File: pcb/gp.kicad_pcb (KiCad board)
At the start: 2 copper layers, 52.1 x 20.3 mm, 33 parts, among them J1 USB_C_Receptacle_USB2.0, U1 XC6206P332MR, U2 STM32F103CBT6, Y1 8M, Y2 NM (32.768k)

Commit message: Hmmmm
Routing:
- net RST: track 46.5 -> 47.6 mm
- net C14: track 34.1 -> 34.7 mm

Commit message: Hmmmm
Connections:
- J4 pad 1: GND -> +3V3
- J4 pad 2: RST -> GND
- J4 pad 3: BO0 -> +5V
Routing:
- net BO0: track 27.0 -> 24.4 mm
- net RST: track 47.6 -> 45.2 mm
- net +3V3: track 141.7 -> 142.5 mm
- net GND: track 0.79 -> 0.00 mm
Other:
- board text removed: "BO0"

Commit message: Hmmm
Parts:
- moved J1 1.27 mm to (200.0, 101.6)
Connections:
- J3 pad 1: GND -> +3V3
- J3 pad 10: A5 -> A4
- J3 pad 11: A6 -> A5
- J3 pad 12: A7 -> A6
- J3 pad 13: B0 -> A7
- J3 pad 14: B1 -> B0
- J3 pad 15: B2 -> B1
- J3 pad 16: B10 -> B2
- J3 pad 17: B11 -> B10
- J3 pad 19: +5V -> GND
- J3 pad 20: GND -> +5V
- J3 pad 5: A0 -> RST
- J3 pad 6: A1 -> A0
- J3 pad 7: A2 -> A1
- J3 pad 8: A3 -> A2
- J3 pad 9: A4 -> A3
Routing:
- net +5V: track 15.0 -> 80.0 mm
- net RST: track 45.2 -> 32.3 mm, vias 4 -> 3
- net B11: track 12.3 -> 0.00 mm
- net +3V3: track 142.5 -> 148.1 mm
- net B2: track 7.57 -> 10.9 mm
- net A4: track 11.0 -> 7.69 mm, vias 1 -> 0
- net VBUS: track 13.7 -> 10.5 mm
- net A5: track 9.07 -> 5.99 mm, vias 1 -> 0
- net A3: track 11.5 -> 8.66 mm
- net A2: track 11.6 -> 9.02 mm
- net Net-(J1-PadA7): track 5.22 -> 7.76 mm
- net A1: track 13.9 -> 11.4 mm
- net A0: track 16.2 -> 13.7 mm
- net B10: track 10.4 -> 12.5 mm
- net B1: track 6.19 -> 7.99 mm
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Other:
- board text removed: "B11"

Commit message: Updated pcb
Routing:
- net A11: track 26.0 -> 27.7 mm
- net A12: track 30.1 -> 31.6 mm

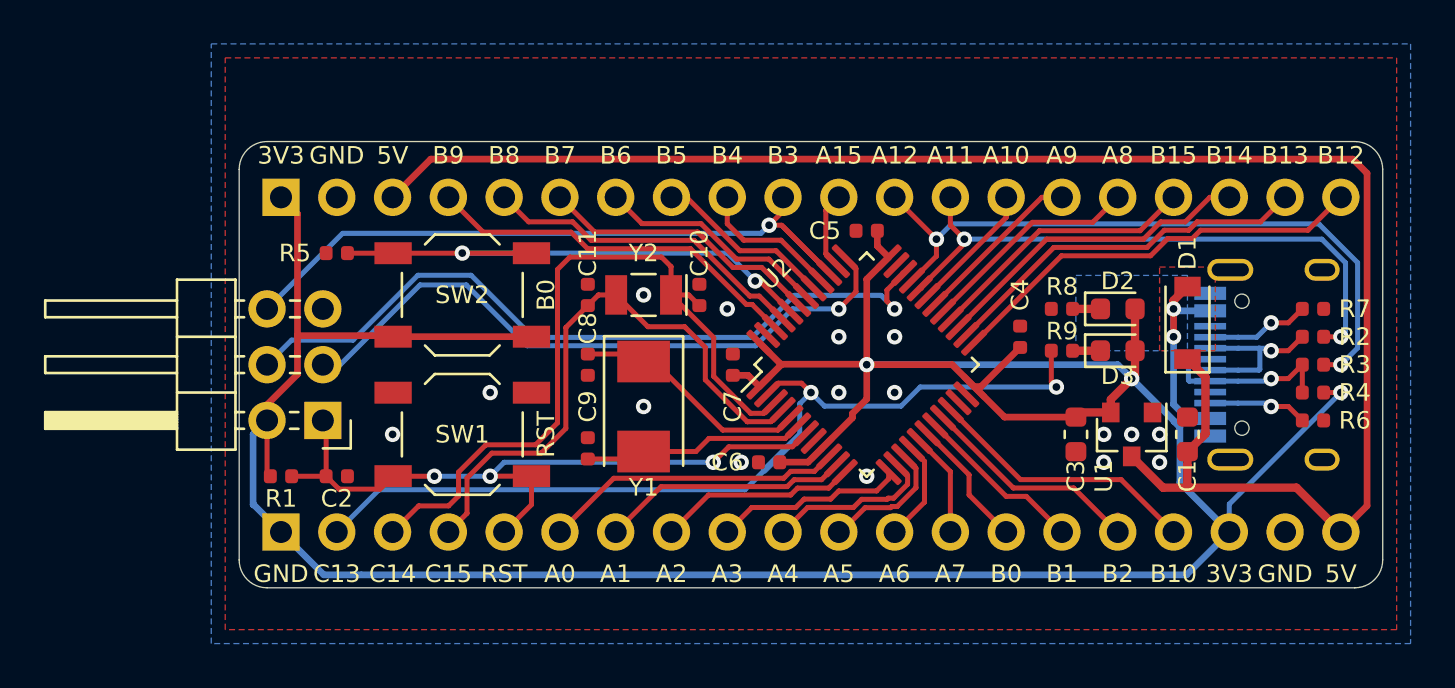
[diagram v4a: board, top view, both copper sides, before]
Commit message: Changed buttons
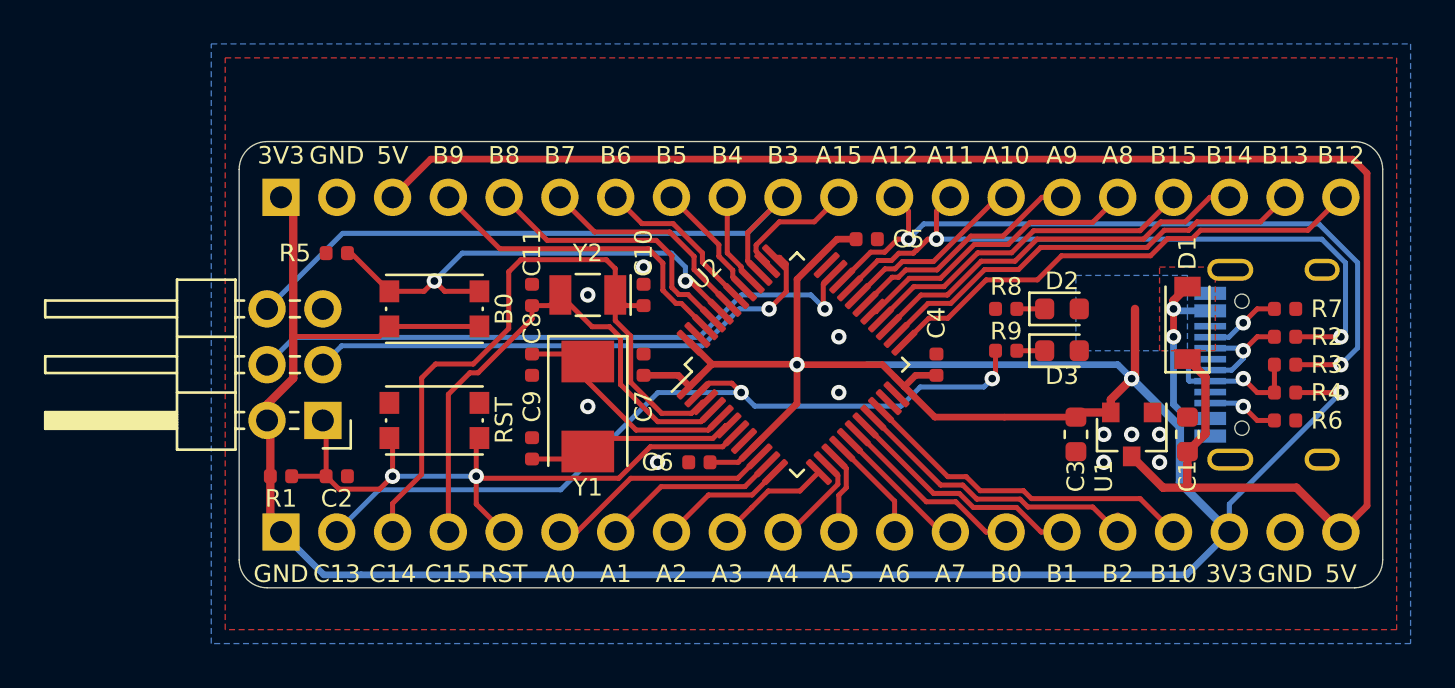
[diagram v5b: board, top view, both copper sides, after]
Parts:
- SW1, SW2: footprint Button_Switch_SMD:SW_SPST_TL3342 -> Button_Switch_SMD:SW_Push_1P1T_NO_CK_KMR2
- moved C7 4.06 mm to (170.2, 101.6)
- moved C4 4.02 mm to (183.5, 101.6)
- moved C6 3.18 mm to (172.7, 106.0)
- moved U2 3.18 mm to (177.2, 101.6)
- moved D2 2.54 mm to (189.2, 99.1)
- moved D3 2.54 mm to (189.2, 101.0)
- moved Y1 2.54 mm to (167.6, 103.5)
- moved Y2 2.54 mm to (167.6, 98.4)
- moved C10 2.54 mm to (170.2, 98.4)
- moved C11 2.54 mm to (165.1, 98.4)
- moved C8 2.54 mm to (165.1, 101.6)
- moved C9 2.54 mm to (165.1, 105.4)
- moved R8 2.54 mm to (186.7, 99.1)
- moved R9 2.54 mm to (186.7, 101.0)
- moved SW1 1.42 mm to (160.7, 104.1)
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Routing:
- net SWDIO: track 34.7 -> 28.9 mm
- net SWCLK: track 29.7 -> 24.4 mm
- net A11: track 27.7 -> 32.0 mm
- net C13: track 41.0 -> 37.0 mm
- net A12: track 31.6 -> 35.1 mm
- net A3: track 8.66 -> 5.31 mm
- net C14: track 34.7 -> 31.4 mm
- net A4: track 7.69 -> 4.52 mm
- net B12: track 19.4 -> 22.6 mm
- net A0: track 13.7 -> 10.5 mm
- net B13: track 17.1 -> 20.3 mm
- net A1: track 11.4 -> 8.18 mm
- net B14: track 14.8 -> 18.0 mm
- net B10: track 12.5 -> 15.7 mm
- net B15: track 12.4 -> 15.6 mm
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
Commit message: Hmmm
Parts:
- J1: moved to F.Cu
- moved R6 7.65 mm to (193.7, 99.1), turned to 180 degrees
- moved R7 7.65 mm to (193.7, 104.1), turned to 180 degrees
- moved D1 6.35 mm to (191.1, 104.8)
- moved R2 6.25 mm to (193.7, 102.9), turned to 180 degrees
- moved R4 6.25 mm to (193.7, 100.3), turned to 180 degrees
- moved C1 5.72 mm to (189.2, 104.8)
- moved C3 5.72 mm to (184.2, 104.8)
- moved U1 5.72 mm to (186.7, 104.8)
- moved R3 5.71 mm to (193.7, 101.6), turned to 180 degrees
- moved R8 1.80 mm to (185.4, 100.3)
- moved R9 1.42 mm to (185.4, 101.6)
- moved D2 1.42 mm to (188.0, 99.7)
- moved D3 1.42 mm to (188.0, 101.6)
- turned J1 to 90 degrees
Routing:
- net +3V3: track 146.8 -> 121.0 mm, vias 3 -> 2
- net A12: track 35.1 -> 23.0 mm, vias 2 -> 1
- net VBUS: track 10.5 -> 0.00 mm, vias 2 -> 0
- net A11: track 32.0 -> 22.2 mm, vias 2 -> 1
- net C13: track 37.0 -> 32.2 mm
- net Net-(D3-Pad1): track 1.27 -> 0.00 mm
- net Net-(D2-Pad1): track 1.27 -> 0.00 mm
- net Net-(J1-PadA6): track 7.44 -> 6.24 mm, vias 1 -> 0
- net Net-(J1-PadB5): track 3.25 -> 2.15 mm, vias 1 -> 0
- net Net-(J1-PadA5): track 3.46 -> 2.54 mm, vias 1 -> 0
- net +5V: track 79.7 -> 80.5 mm
- net Net-(J1-PadA7): track 5.32 -> 4.80 mm, vias 1 -> 0

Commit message: Rev c ready to order - production files gp_c verified.
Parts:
- moved R8 2.29 mm to (186.7, 98.4)
- moved D1 2.01 mm to (193.0, 105.4)
- moved R2 1.91 mm to (193.7, 101.0)
- moved R3 1.91 mm to (193.7, 99.7)
- moved R4 1.91 mm to (193.7, 98.4)
- moved R6 1.91 mm to (193.7, 97.2)
- moved R7 1.91 mm to (193.7, 102.2)
- moved R9 1.80 mm to (186.7, 100.3)
- moved D2 1.80 mm to (189.2, 98.4)
- moved D3 1.80 mm to (189.2, 100.3)
- moved C1 1.42 mm to (190.5, 104.1)
- moved U1 1.42 mm to (188.0, 104.1)
- moved C3 1.42 mm to (185.4, 104.1)
- moved C7 0.63 mm to (170.8, 101.6)
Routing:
- net +3V3: track 121.0 -> 109.0 mm, vias 2 -> 3
- net VBUS: track 0.00 -> 10.3 mm, vias 0 -> 3
- net C13: track 32.2 -> 35.3 mm
- net Net-(J1-PadB5): track 2.15 -> 4.01 mm
- net Net-(D3-Pad1): track 0.00 -> 1.27 mm
- net Net-(D2-Pad1): track 0.00 -> 1.27 mm
- net A12: track 23.0 -> 22.2 mm
- net +5V: track 80.5 -> 79.7 mm
- net B7: track 10.0 -> 10.7 mm
- net B6: track 7.60 -> 8.28 mm
- net A11: track 22.2 -> 22.8 mm
- net GND: vias 11 -> 15

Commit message: Order rev c
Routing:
- net A12: track 22.2 -> 21.3 mm
- net A11: track 22.8 -> 22.1 mm
